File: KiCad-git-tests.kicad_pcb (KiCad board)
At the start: 2 copper layers, 23 x 11.8 mm, 2 parts

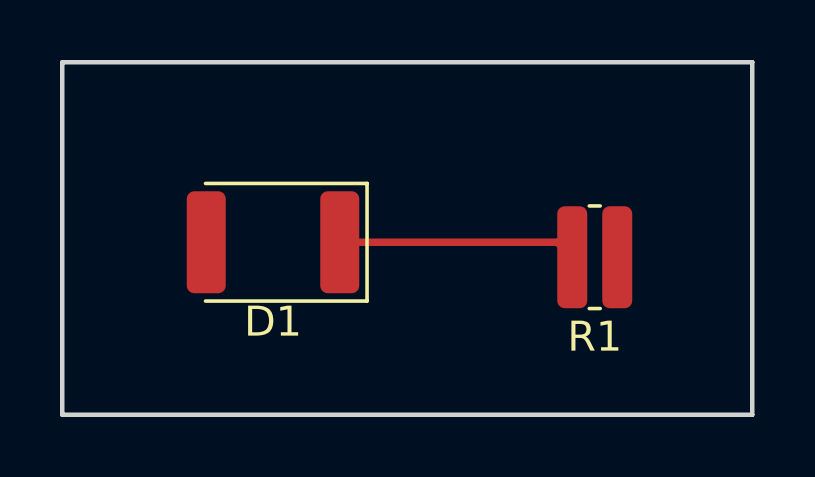
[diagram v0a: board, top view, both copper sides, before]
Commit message: duplicate resistor
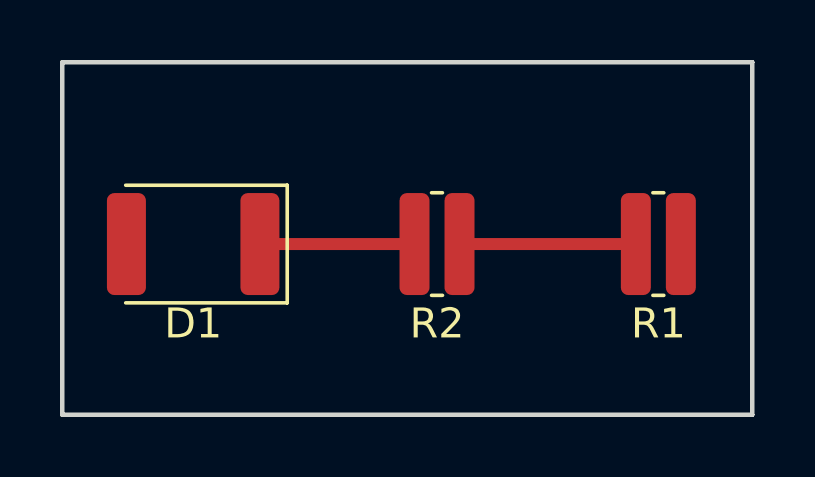
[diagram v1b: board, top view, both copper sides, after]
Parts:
- added R2: R, Resistor_SMD:R_0612_1632Metric, F.Cu at (67.7, 40.3)
- moved D1 2.66 mm to (59.6, 40.3)
- moved R1 2.17 mm to (75.1, 40.3)
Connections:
- R1 pad 2: Net-(D1-KA) -> Net-(R1-Pad2)
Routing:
- net Net-(R1-Pad2): track 0.00 -> 5.88 mm
- net Net-(D1-KA): track 7.96 -> 5.15 mm
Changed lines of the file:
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@@
 	(footprint "Resistor_SMD:R_0612_1632Metric"
 		(layer "F.Cu")
-		(at 73 40.75 180)
+		(at 67.742 40.31 180)
 		(descr "Resistor SMD 0612 (1632 Metric), square (rectangular) end terminal, IPC-7351 nominal, (Body size source: https://www.vishay.com/docs/20019/rcwe.pdf)")
 		(tags "resistor")
-		(property "Reference" "R1"
+		(property "Reference" "R2"
 			(at 0 -2.65 0)
 			(layer "F.SilkS")
@@
 			(layers "F.Cu" "F.Mask" "F.Paste")
 			(roundrect_rratio 0.25)
-			(net "+5V")
+			(net "Net-(R1-Pad2)")
 			(pintype "passive")
 		)
@@
 		)
 	)
+	(footprint "Resistor_SMD:R_0612_1632Metric"
+		(layer "F.Cu")
+		(at 75.12 40.31 180)
+		(descr "Resistor SMD 0612 (1632 Metric), square (rectangular) end terminal, IPC-7351 nominal, (Body size source: https://www.vishay.com/docs/20019/rcwe.pdf)")
+		(tags "resistor")
+		(property "Reference" "R1"
+			(at 0 -2.65 0)
+			(layer "F.SilkS")
+			(effects
+				(font
+					(size 1 1)
+					(thickness 0.15)
+				)
+			)
+		)
+		(property "Value" "R"
+			(at 0 2.65 0)
+			(layer "F.Fab")
+			(effects
+				(font
+					(size 1 1)
+					(thickness 0.15)
+				)
+			)
+		)
+		(property "Datasheet" ""
+			(at 0 0 0)
+			(layer "F.Fab")
+			(hide yes)
+			(effects
+				(font
+					(size 1.27 1.27)
+				)
+			)
+		)
+		(property "Description" "Resistor"
+			(at 0 0 0)
+			(layer "F.Fab")
+			(hide yes)
+			(effects
+				(font
+					(size 1.27 1.27)
+				)
+			)
+		)
+		(property "KiLib_Generator" "SMD_2terminal_chip_molded"
+			(at 0 0 0)
+			(layer "F.SilkS")
+			(hide yes)
+			(effects
+				(font
+					(size 1 1)
+					(thickness 0.15)
+				)
+			)
+		)
+		(property ki_fp_filters "R_*")
+		(sheetname "/")
+		(sheetfile "KiCad-git-tests.kicad_sch")
+		(units
+			(unit
+				(name "A")
+				(pins "1" "2")
+			)
+		)
+		(attr smd)
+		(duplicate_pad_numbers_are_jumpers no)
+		(fp_line
+			(start -0.182983 1.71)
+			(end 0.182983 1.71)
+			(stroke
+				(width 0.12)
+				(type solid)
+			)
+			(layer "F.SilkS")
+		)
+		(fp_line
+			(start -0.182983 -1.71)
+			(end 0.182983 -1.71)
+			(stroke
+				(width 0.12)
+				(type solid)
+			)
+			(layer "F.SilkS")
+		)
+		(fp_rect
+			(start -1.5 -1.95)
+			(end 1.5 1.95)
+			(stroke
+				(width 0.05)
+				(type solid)
+			)
+			(fill no)
+			(layer "F.CrtYd")
+		)
+		(fp_rect
+			(start -0.8 -1.6)
+			(end 0.8 1.6)
+			(stroke
+				(width 0.1)
+				(type solid)
+			)
+			(fill no)
+			(layer "F.Fab")
+		)
+		(fp_text user "${REFERENCE}"
+			(at 0 0 0)
+			(layer "F.Fab")
+			(effects
+				(font
+					(size 0.4 0.4)
+					(thickness 0.06)
+				)
+			)
+		)
+		(pad "1" smd roundrect
+			(at -0.75 0 180)
+			(size 1 3.4)
+			(layers "F.Cu" "F.Mask" "F.Paste")
+			(roundrect_rratio 0.25)
+			(net "+5V")
+			(pintype "passive")
+		)
+		(pad "2" smd roundrect
+			(at 0.75 0 180)
+			(size 1 3.4)
+			(layers "F.Cu" "F.Mask" "F.Paste")
+			(roundrect_rratio 0.25)
+			(net "Net-(R1-Pad2)")
+			(pintype "passive")
+		)
+		(embedded_fonts no)
+		(model "${KICAD10_3DMODEL_DIR}/Resistor_SMD.3dshapes/R_0612_1632Metric.step"
+			(offset
+				(xyz 0 0 0)
+			)
+			(scale
+				(xyz 1 1 1)
+			)
+			(rotate
+				(xyz 0 0 0)
+			)
+		)
+	)
 	(footprint "LED_SMD:LED_1812_4532Metric_Pad1.30x3.40mm_HandSolder"
 		(layer "F.Cu")
-		(at 62.275 40.25 180)
+		(at 59.614 40.31 180)
 		(descr "LED SMD 1812 (4532 Metric), square (rectangular) end terminal, IPC-7351 nominal, (Body size source: https://www.nikhef.nl/pub/departments/mt/projects/detectorR_D/dtddice/ERJ2G.pdf)")
 		(tags "LED handsolder")
@@
 	)
 	(segment
-		(start 64.5 40.25)
-		(end 71.75 40.25)
-		(width 0.25)
+		(start 66.992 40.31)
+		(end 61.839 40.31)
+		(width 0.4)
 		(layer "F.Cu")
 		(net "Net-(D1-KA)")
 	)
 	(segment
-		(start 71.75 40.25)
-		(end 72.25 40.75)
-		(width 0.25)
+		(start 74.37 40.31)
+		(end 68.492 40.31)
+		(width 0.4)
 		(layer "F.Cu")
-		(net "Net-(D1-KA)")
+		(net "Net-(R1-Pad2)")
 	)
 	(embedded_fonts no)
